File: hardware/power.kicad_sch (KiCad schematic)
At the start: 27 parts, among them J7 12401610E4#2A, Q1 DMG2307L, Q2 DMG2307L, Q3 BSD235N, U7 AP9101CK, U8 MIC5504-3.3YM5

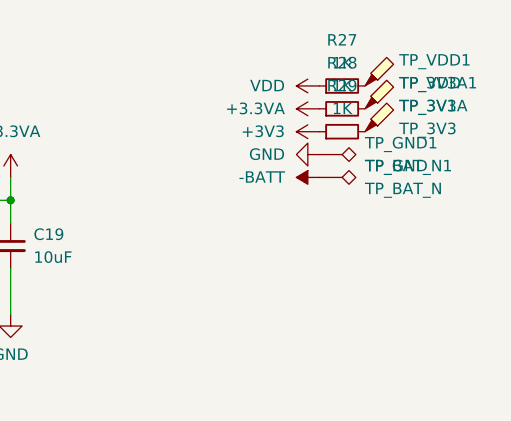
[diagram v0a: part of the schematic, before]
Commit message: Added test point
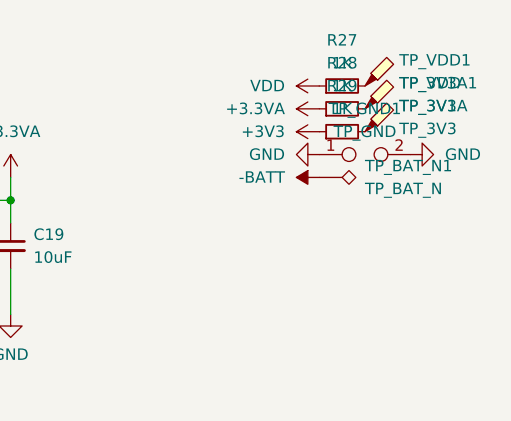
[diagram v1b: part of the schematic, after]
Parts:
- removed TP_GND1: TP_GND, TestPoint:TestPoint_Pad_D1.5mm, symbol Connector:TestPoint_Alt
- added TP_GND1: TP_GND, Resistor_SMD:R_0805_2012Metric, symbol Connector:TestPoint_2Pole
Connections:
- net GND: now also TP_GND1.1, TP_GND1.2
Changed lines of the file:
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@@
 		(length 2.54)
 		(shape round)
-		(at 220.98 31.75 0)
-		(fields_autoplaced yes)
-		(effects
-			(font
-				(size 1.27 1.27)
-			)
-			(justify left bottom)
-		)
-		(property "Netclass" "Powergrid"
-			(at 221.6785 29.21 0)
-			(effects
-				(font
-					(size 1.27 1.27)
-				)
-				(justify left)
-			)
-		)
-		(property "Component Class" ""
-			(at 58.42 -53.34 0)
-			(effects
-				(font
-					(size 1.27 1.27)
-					(italic yes)
-				)
-			)
-		)
-	)
-	(netclass_flag ""
-		(length 2.54)
-		(shape round)
 		(at 134.62 43.18 0)
 		(fields_autoplaced yes)
@@
 	)
 	(symbol
-		(lib_id "Connector:TestPoint_Alt")
-		(at 266.7 26.67 270)
-		(unit 1)
-		(exclude_from_sim no)
-		(in_bom yes)
-		(on_board yes)
-		(dnp no)
-		(fields_autoplaced yes)
-		(property "Reference" "TP_GND1"
-			(at 271.78 25.3999 90)
-			(effects
-				(font
-					(size 1.27 1.27)
-				)
-				(justify left)
-			)
-		)
-		(property "Value" "TP_GND"
-			(at 271.78 27.9399 90)
-			(effects
-				(font
-					(size 1.27 1.27)
-				)
-				(justify left)
-			)
-		)
-		(property "Footprint" "TestPoint:TestPoint_Pad_D1.5mm"
-			(at 266.7 31.75 0)
-			(effects
-				(font
-					(size 1.27 1.27)
-				)
-				(hide yes)
-			)
-		)
-		(property "Datasheet" "~"
-			(at 266.7 31.75 0)
-			(effects
-				(font
-					(size 1.27 1.27)
-				)
-				(hide yes)
-			)
-		)
-		(property "Description" "test point (alternative shape)"
-			(at 266.7 26.67 0)
-			(effects
-				(font
-					(size 1.27 1.27)
-				)
-				(hide yes)
-			)
-		)
-		(pin "1"
-		)
-		(instances
-			(project ""
-				(path "/adf38c8f-bada-4838-acc6-e6af19946742/8a4812e6-01d2-4a59-bc73-706ba54f858f"
-					(reference "TP_GND1")
-					(unit 1)
-				)
-			)
-		)
-	)
-	(symbol
 		(lib_id "Device:R_Small")
 		(at 85.09 95.25 270)
@@
 	(symbol
 		(lib_id "power:GND")
+		(at 276.86 26.67 90)
+		(unit 1)
+		(exclude_from_sim no)
+		(in_bom yes)
+		(on_board yes)
+		(dnp no)
+		(fields_autoplaced yes)
+		(property "Reference" "#PWR04"
+			(at 283.21 26.67 0)
+			(effects
+				(font
+					(size 1.27 1.27)
+				)
+				(hide yes)
+			)
+		)
+		(property "Value" "GND"
+			(at 280.67 26.6699 90)
+			(effects
+				(font
+					(size 1.27 1.27)
+				)
+				(justify right)
+			)
+		)
+		(property "Footprint" ""
+			(at 276.86 26.67 0)
+			(effects
+				(font
+					(size 1.27 1.27)
+				)
+				(hide yes)
+			)
+		)
+		(property "Datasheet" ""
+			(at 276.86 26.67 0)
+			(effects
+				(font
+					(size 1.27 1.27)
+				)
+				(hide yes)
+			)
+		)
+		(property "Description" "Power symbol creates a global label with name \"GND\" , ground"
+			(at 276.86 26.67 0)
+			(effects
+				(font
+					(size 1.27 1.27)
+				)
+				(hide yes)
+			)
+		)
+		(pin "1"
+		)
+		(instances
+			(project "Scale"
+				(path "/adf38c8f-bada-4838-acc6-e6af19946742/8a4812e6-01d2-4a59-bc73-706ba54f858f"
+					(reference "#PWR04")
+					(unit 1)
+				)
+			)
+		)
+	)
+	(symbol
+		(lib_id "power:GND")
 		(at 184.15 104.14 270)
 		(unit 1)
@@
 				)
 			)
+		)
+	)
+	(symbol
+		(lib_id "Connector:TestPoint_2Pole")
+		(at 271.78 26.67 0)
+		(unit 1)
+		(exclude_from_sim no)
+		(in_bom yes)
+		(on_board yes)
+		(dnp no)
+		(fields_autoplaced yes)
+		(property "Reference" "TP_GND1"
+			(at 271.78 21.59 0)
+			(effects
+				(font
+					(size 1.27 1.27)
+				)
+			)
+		)
+		(property "Value" "TP_GND"
+			(at 271.78 24.13 0)
+			(effects
+				(font
+					(size 1.27 1.27)
+				)
+			)
+		)
+		(property "Footprint" "Resistor_SMD:R_0805_2012Metric"
+			(at 271.78 26.67 0)
+			(effects
+				(font
+					(size 1.27 1.27)
+				)
+				(hide yes)
+			)
+		)
+		(property "Datasheet" "~"
+			(at 271.78 26.67 0)
+			(effects
+				(font
+					(size 1.27 1.27)
+				)
+				(hide yes)
+			)
+		)
+		(property "Description" "2-polar test point"
+			(at 271.78 26.67 0)
+			(effects
+				(font
+					(size 1.27 1.27)
+				)
+				(hide yes)
+			)
+		)
+		(pin "2"
+		)
+		(pin "1"
+		)
+		(instances
+			(project ""
+				(path "/adf38c8f-bada-4838-acc6-e6af19946742/8a4812e6-01d2-4a59-bc73-706ba54f858f"
+					(reference "TP_GND1")
+					(unit 1)
+				)
+			)
